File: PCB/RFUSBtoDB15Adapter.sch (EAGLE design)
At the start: 24 parts, among them IC1 S-816A40AMC-BAPT2U, J1 0, J2 AVR_SPI_PROG_3X2NS, Q2 2SA1213-Y(TE12L,F)

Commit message: PCB
PCB design updated
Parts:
- removed JP1: (no value), jumper:JP2E
- removed SJ3: (no value), jumper:SJ
- added C3, C4: 10uF, SparkFun-Capacitors:10UF-POLAR-EIA3216-16V-10%(TANT)
- R1: value 33Ω -> 80R; device eagle-ltspice:R -> SparkFun-Resistors:0.3OHM-0805-1/8W-1%
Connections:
- removed net VBUS: C1.2, C5.+, JP2.1, LED.A, R1.1
- removed net VCCIN: ARDUINO-ATMEGA328P.RAW, J1.2, J2.2, JP1.2
- new net 5VLED: LED.A, R1.1
- net 3.3V: now also ARDUINO-ATMEGA328P.VCC, C4.+; no longer JP1.3
- net 5VREG: now also C1.2, C3.+, C5.+, J1.2, J2.2, JP2.1; no longer JP1.1, SJ3.1, SJ3.2
- net GND: now also C3.-, C4.-

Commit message: PCB update
Small changes
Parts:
- renumbered ARDUINO-ATMEGA328P to ARDUINO-MINIPRO
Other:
- note removed: "IF USING A 5V ARDUINO, FEED RAW (VCCIN) PIN WITH 3.3V FROM THE REGULATOR (REG1117)."
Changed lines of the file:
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@@
 </classes>
 <parts>
-<part name="ARDUINO-ATMEGA328P" library="Arduino" deviceset="ARDUINO-PRO-MINI-*" device="" technology="5.0V"/>
+<part name="ARDUINO-MINIPRO" library="Arduino" deviceset="ARDUINO-PRO-MINI-*" device="" technology="5.0V"/>
 <part name="DB15OUT" library="dbconnector" deviceset="DB15M/90" device="" value="0"/>
 <part name="3.3V" library="burr-brown" library_urn="urn:adsk.eagle:library:111" deviceset="REG1117" device="" package3d_urn="urn:adsk.eagle:package:4940/1"/>
@@
 <sheet>
 <plain>
-<text x="45.212" y="-6.35" size="1.524" layer="113" distance="67" align="top-left">IF USING A 5V ARDUINO, FEED
-RAW (VCCIN) PIN WITH 3.3V
-FROM THE REGULATOR (REG1117).</text>
-<rectangle x1="42.418" y1="-16.002" x2="83.058" y2="-3.302" layer="203"/>
-<text x="45.72" y="-17.018" size="1.524" layer="113" distance="67" align="top-left">THE 5V REGULATOR (IC1) WILL
+<text x="-25.4" y="-17.018" size="1.524" layer="113" distance="67" align="top-left">THE 5V REGULATOR (IC1) WILL
 PROTECT THE VCC LINE FROM
 A POSSIBLE BAD PSU VOLTAGE,
 IF YOU DON'T NEED, JUST JUMPER
 SJ1.</text>
-<rectangle x1="42.418" y1="-29.21" x2="83.058" y2="-16.51" layer="203"/>
+<rectangle x1="-28.702" y1="-29.21" x2="11.938" y2="-16.51" layer="203"/>
 <text x="-46.482" y="50.546" size="1.524" layer="113" distance="67" align="top-left">FEED USB HOST SHIELD MINI VBUS WITH JP2</text>
 <rectangle x1="-49.276" y1="45.72" x2="4.064" y2="53.34" layer="203"/>
 </plain>
 <instances>
-<instance part="ARDUINO-ATMEGA328P" gate="G$1" x="-104.14" y="71.12" smashed="yes" rot="R180">
+<instance part="ARDUINO-MINIPRO" gate="G$1" x="-104.14" y="71.12" smashed="yes" rot="R180">
 <attribute name="NAME" x="-117.856" y="102.362" size="1.778" layer="95"/>
 </instance>
@@
 <instance part="C5" gate="G$1" x="9.398" y="77.47" smashed="yes" rot="R90">
 <attribute name="NAME" x="8.763" y="78.486" size="1.778" layer="95" rot="R90"/>
-<attribute name="VALUE" x="11.684" y="75.565" size="1.778" layer="96"/>
+<attribute name="VALUE" x="11.684" y="80.645" size="1.778" layer="96"/>
 </instance>
 <instance part="LOGO1" gate="G$1" x="-142.24" y="-20.32" smashed="yes"/>
@@
 </segment>
 <segment>
-<pinref part="ARDUINO-ATMEGA328P" gate="G$1" pin="D2"/>
+<pinref part="ARDUINO-MINIPRO" gate="G$1" pin="D2"/>
 <wire x1="-86.36" y1="68.58" x2="-68.58" y2="68.58" width="0.1524" layer="91"/>
 <label x="-68.58" y="68.58" size="1.778" layer="95"/>
@@
 </segment>
 <segment>
-<pinref part="ARDUINO-ATMEGA328P" gate="G$1" pin="D3"/>
+<pinref part="ARDUINO-MINIPRO" gate="G$1" pin="D3"/>
 <wire x1="-86.36" y1="71.12" x2="-68.58" y2="71.12" width="0.1524" layer="91"/>
 <label x="-68.58" y="71.12" size="1.778" layer="95"/>
@@
 </segment>
 <segment>
-<pinref part="ARDUINO-ATMEGA328P" gate="G$1" pin="D4"/>
+<pinref part="ARDUINO-MINIPRO" gate="G$1" pin="D4"/>
 <wire x1="-86.36" y1="73.66" x2="-68.58" y2="73.66" width="0.1524" layer="91"/>
 <label x="-68.58" y="73.66" size="1.778" layer="95"/>
@@
 </segment>
 <segment>
-<pinref part="ARDUINO-ATMEGA328P" gate="G$1" pin="A3"/>
+<pinref part="ARDUINO-MINIPRO" gate="G$1" pin="A3"/>
 <wire x1="-121.92" y1="68.58" x2="-139.7" y2="68.58" width="0.1524" layer="91"/>
 <label x="-142.24" y="68.58" size="1.778" layer="95"/>
@@
 <segment>
 <wire x1="-139.7" y1="71.12" x2="-121.92" y2="71.12" width="0.1524" layer="91"/>
-<pinref part="ARDUINO-ATMEGA328P" gate="G$1" pin="A2"/>
+<pinref part="ARDUINO-MINIPRO" gate="G$1" pin="A2"/>
 <label x="-144.78" y="71.12" size="1.778" layer="95"/>
 </segment>
@@
 <segment>
 <wire x1="-139.7" y1="73.66" x2="-121.92" y2="73.66" width="0.1524" layer="91"/>
-<pinref part="ARDUINO-ATMEGA328P" gate="G$1" pin="A1"/>
+<pinref part="ARDUINO-MINIPRO" gate="G$1" pin="A1"/>
 <label x="-144.78" y="73.66" size="1.778" layer="95"/>
 </segment>
@@
 <segment>
 <wire x1="-139.7" y1="76.2" x2="-121.92" y2="76.2" width="0.1524" layer="91"/>
-<pinref part="ARDUINO-ATMEGA328P" gate="G$1" pin="A0"/>
+<pinref part="ARDUINO-MINIPRO" gate="G$1" pin="A0"/>
 <label x="-144.78" y="76.2" size="1.778" layer="95"/>
 </segment>
@@
 </segment>
 <segment>
-<pinref part="ARDUINO-ATMEGA328P" gate="G$1" pin="A5"/>
+<pinref part="ARDUINO-MINIPRO" gate="G$1" pin="A5"/>
 <wire x1="-121.92" y1="50.8" x2="-142.24" y2="50.8" width="0.1524" layer="91"/>
 <label x="-149.86" y="50.8" size="1.778" layer="95"/>
 </segment>
 <segment>
-<pinref part="ARDUINO-ATMEGA328P" gate="G$1" pin="GND.3"/>
+<pinref part="ARDUINO-MINIPRO" gate="G$1" pin="GND.3"/>
 <wire x1="-121.92" y1="96.52" x2="-134.62" y2="96.52" width="0.1524" layer="91"/>
 <label x="-134.62" y="96.52" size="1.778" layer="95"/>
@@
 <net name="BUT4" class="0">
 <segment>
-<pinref part="ARDUINO-ATMEGA328P" gate="G$1" pin="D5"/>
+<pinref part="ARDUINO-MINIPRO" gate="G$1" pin="D5"/>
 <wire x1="-86.36" y1="76.2" x2="-68.58" y2="76.2" width="0.1524" layer="91"/>
 <label x="-68.58" y="76.2" size="1.778" layer="95"/>
@@
 </segment>
 <segment>
-<pinref part="ARDUINO-ATMEGA328P" gate="G$1" pin="D6"/>
+<pinref part="ARDUINO-MINIPRO" gate="G$1" pin="D6"/>
 <wire x1="-86.36" y1="78.74" x2="-68.58" y2="78.74" width="0.1524" layer="91"/>
 <label x="-68.58" y="78.74" size="1.778" layer="95"/>
@@
 <net name="BUT5" class="0">
 <segment>
-<pinref part="ARDUINO-ATMEGA328P" gate="G$1" pin="D7"/>
+<pinref part="ARDUINO-MINIPRO" gate="G$1" pin="D7"/>
 <wire x1="-86.36" y1="81.28" x2="-68.58" y2="81.28" width="0.1524" layer="91"/>
 <label x="-68.58" y="81.28" size="1.778" layer="95"/>
@@
 </segment>
 <segment>
-<pinref part="ARDUINO-ATMEGA328P" gate="G$1" pin="VCC"/>
+<pinref part="ARDUINO-MINIPRO" gate="G$1" pin="VCC"/>
 <wire x1="-121.92" y1="66.04" x2="-139.7" y2="66.04" width="0.1524" layer="91"/>
 <label x="-140.208" y="66.04" size="1.778" layer="95"/>
@@
 <net name="BUT6" class="0">
 <segment>
-<pinref part="ARDUINO-ATMEGA328P" gate="G$1" pin="A4"/>
+<pinref part="ARDUINO-MINIPRO" gate="G$1" pin="A4"/>
 <wire x1="-121.92" y1="53.34" x2="-142.24" y2="53.34" width="0.1524" layer="91"/>
 <label x="-149.86" y="53.34" size="1.778" layer="95"/>
@@
 </segment>
 <segment>
-<pinref part="ARDUINO-ATMEGA328P" gate="G$1" pin="P_GND"/>
+<pinref part="ARDUINO-MINIPRO" gate="G$1" pin="P_GND"/>
 <wire x1="-109.22" y1="35.56" x2="-109.22" y2="27.94" width="0.1524" layer="91"/>
 <label x="-109.22" y="22.86" size="1.778" layer="95" rot="R90"/>
 </segment>
 <segment>
-<pinref part="ARDUINO-ATMEGA328P" gate="G$1" pin="GND.1"/>
+<pinref part="ARDUINO-MINIPRO" gate="G$1" pin="GND.1"/>
 <wire x1="-86.36" y1="66.04" x2="-68.58" y2="66.04" width="0.1524" layer="91"/>
 <label x="-68.58" y="66.04" size="1.778" layer="95"/>
 </segment>
 <segment>
-<pinref part="ARDUINO-ATMEGA328P" gate="G$1" pin="GND.2"/>
+<pinref part="ARDUINO-MINIPRO" gate="G$1" pin="GND.2"/>
 <wire x1="-121.92" y1="60.96" x2="-142.24" y2="60.96" width="0.1524" layer="91"/>
 <label x="-147.32" y="60.96" size="1.778" layer="95"/>
@@
 <wire x1="-96.52" y1="35.56" x2="-96.52" y2="27.94" width="0.1524" layer="91"/>
 <label x="-97.028" y="27.94" size="1.778" layer="95" rot="R270"/>
-<pinref part="ARDUINO-ATMEGA328P" gate="G$1" pin="P_DTR"/>
+<pinref part="ARDUINO-MINIPRO" gate="G$1" pin="P_DTR"/>
 </segment>
 </net>
 <net name="TX" class="0">
 <segment>
-<pinref part="ARDUINO-ATMEGA328P" gate="G$1" pin="P_TXD"/>
+<pinref part="ARDUINO-MINIPRO" gate="G$1" pin="P_TXD"/>
 <wire x1="-99.06" y1="35.56" x2="-99.06" y2="27.94" width="0.1524" layer="91"/>
 <label x="-98.298" y="24.892" size="1.778" layer="95" rot="R90"/>
@@
 <net name="RX" class="0">
 <segment>
-<pinref part="ARDUINO-ATMEGA328P" gate="G$1" pin="P_RXD"/>
+<pinref part="ARDUINO-MINIPRO" gate="G$1" pin="P_RXD"/>
 <wire x1="-101.6" y1="35.56" x2="-101.6" y2="27.94" width="0.1524" layer="91"/>
 <label x="-100.584" y="24.638" size="1.778" layer="95" rot="R90"/>
@@
 <net name="RESET" class="0">
 <segment>
-<pinref part="ARDUINO-ATMEGA328P" gate="G$1" pin="RST.1"/>
+<pinref part="ARDUINO-MINIPRO" gate="G$1" pin="RST.1"/>
 <wire x1="-86.36" y1="63.5" x2="-68.58" y2="63.5" width="0.1524" layer="91"/>
 <label x="-68.58" y="63.5" size="1.778" layer="95"/>
@@
 <net name="SCK" class="0">
 <segment>
-<pinref part="ARDUINO-ATMEGA328P" gate="G$1" pin="D13"/>
+<pinref part="ARDUINO-MINIPRO" gate="G$1" pin="D13"/>
 <wire x1="-121.92" y1="78.74" x2="-127" y2="78.74" width="0.1524" layer="91"/>
 <label x="-132.08" y="78.74" size="1.778" layer="95"/>
@@
 <segment>
 <wire x1="-121.92" y1="81.28" x2="-127" y2="81.28" width="0.1524" layer="91"/>
-<pinref part="ARDUINO-ATMEGA328P" gate="G$1" pin="D12"/>
+<pinref part="ARDUINO-MINIPRO" gate="G$1" pin="D12"/>
 <label x="-132.08" y="81.28" size="1.778" layer="95"/>
 </segment>
@@
 <segment>
 <wire x1="-121.92" y1="83.82" x2="-127" y2="83.82" width="0.1524" layer="91"/>
-<pinref part="ARDUINO-ATMEGA328P" gate="G$1" pin="D11"/>
+<pinref part="ARDUINO-MINIPRO" gate="G$1" pin="D11"/>
 <label x="-132.08" y="83.82" size="1.778" layer="95"/>
 </segment>
@@
 <net name="LED" class="0">
 <segment>
-<pinref part="ARDUINO-ATMEGA328P" gate="G$1" pin="D10"/>
+<pinref part="ARDUINO-MINIPRO" gate="G$1" pin="D10"/>
 <wire x1="-121.92" y1="86.36" x2="-134.62" y2="86.36" width="0.1524" layer="91"/>
 <label x="-134.62" y="86.36" size="1.778" layer="95"/>

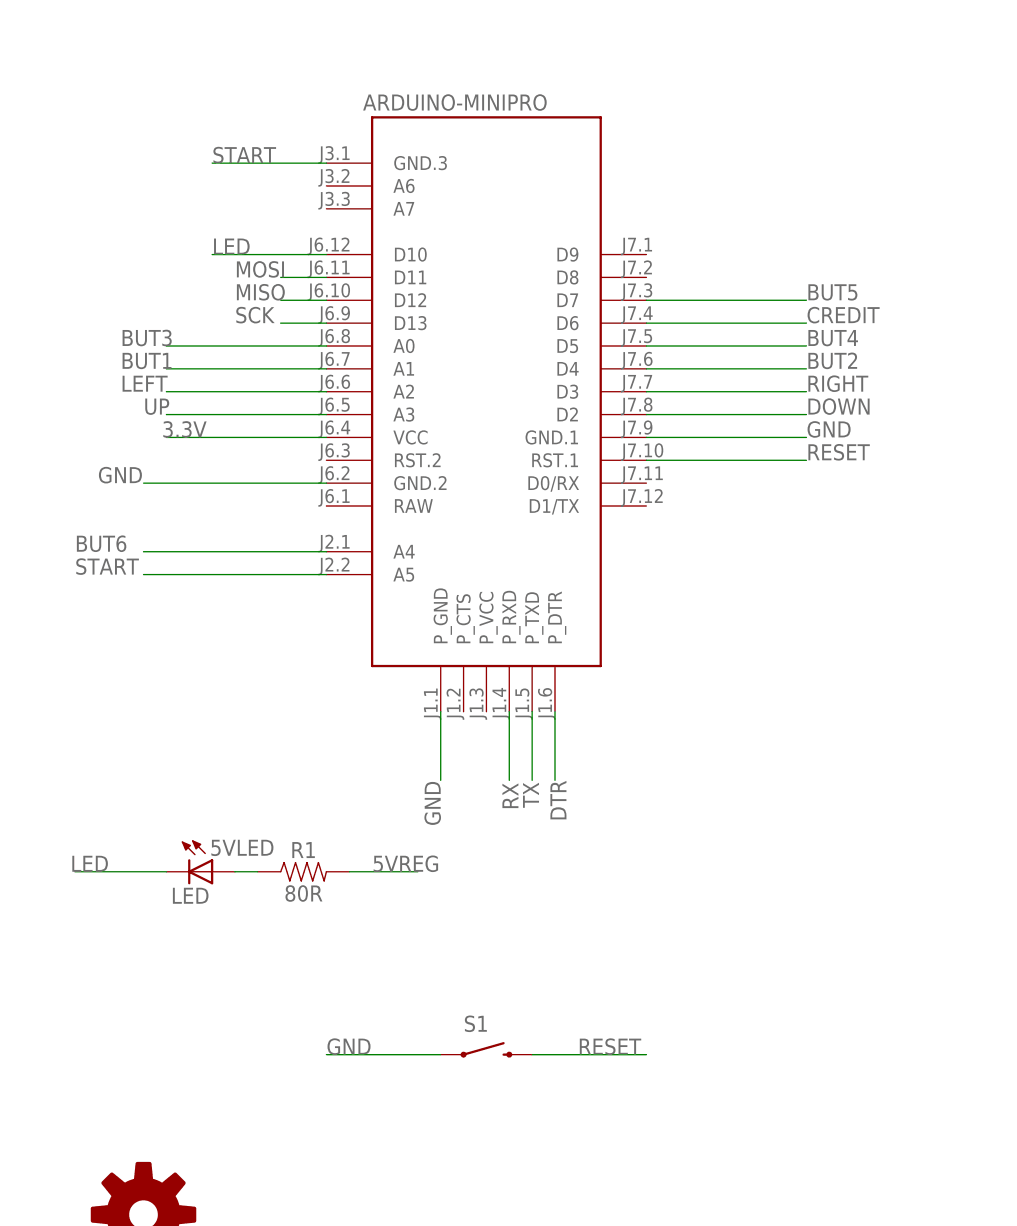
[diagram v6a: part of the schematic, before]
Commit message: PCB Update
LED status and MEMORY RESET now supported
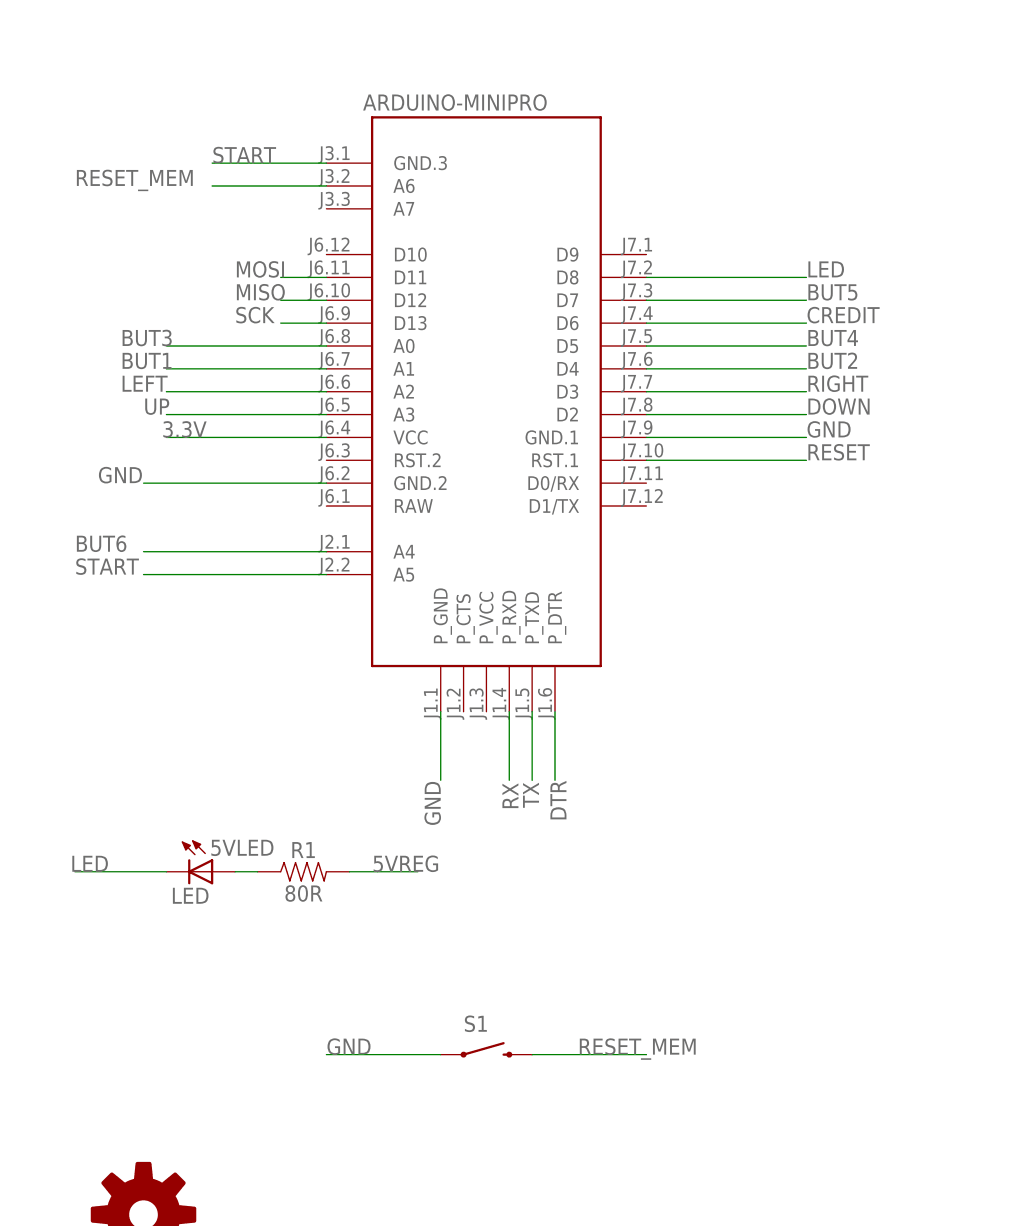
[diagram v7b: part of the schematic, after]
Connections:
- new net RESET_MEM: ARDUINO-MINIPRO.A6, S1.2
- net LED: now also ARDUINO-MINIPRO.D8; no longer ARDUINO-MINIPRO.D10
- net RESET: no longer S1.2
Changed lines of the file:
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@@
 <label x="-121.92" y="-45.72" size="1.778" layer="95"/>
-</segment>
-<segment>
-<pinref part="S1" gate="G$1" pin="2"/>
-<wire x1="-99.06" y1="-2.54" x2="-86.36" y2="-2.54" width="0.1524" layer="91"/>
-<label x="-93.98" y="-2.54" size="1.778" layer="95"/>
 </segment>
 </net>
@@
 <net name="LED" class="0">
 <segment>
-<pinref part="ARDUINO-MINIPRO" gate="G$1" pin="D10"/>
-<wire x1="-121.92" y1="86.36" x2="-134.62" y2="86.36" width="0.1524" layer="91"/>
-<label x="-134.62" y="86.36" size="1.778" layer="95"/>
-</segment>
-<segment>
 <pinref part="LED" gate="G$1" pin="C"/>
 <wire x1="-139.7" y1="17.78" x2="-149.86" y2="17.78" width="0.1524" layer="91"/>
 <label x="-150.368" y="17.78" size="1.778" layer="95"/>
+</segment>
+<segment>
+<pinref part="ARDUINO-MINIPRO" gate="G$1" pin="D8"/>
+<wire x1="-86.36" y1="83.82" x2="-68.58" y2="83.82" width="0.1524" layer="91"/>
+<label x="-68.58" y="83.82" size="1.778" layer="95"/>
 </segment>
 </net>
@@
 </segment>
 </net>
+<net name="RESET_MEM" class="0">
+<segment>
+<pinref part="ARDUINO-MINIPRO" gate="G$1" pin="A6"/>
+<wire x1="-121.92" y1="93.98" x2="-134.62" y2="93.98" width="0.1524" layer="91"/>
+<label x="-149.86" y="93.98" size="1.778" layer="95"/>
+</segment>
+<segment>
+<pinref part="S1" gate="G$1" pin="2"/>
+<wire x1="-99.06" y1="-2.54" x2="-86.36" y2="-2.54" width="0.1524" layer="91"/>
+<label x="-93.98" y="-2.54" size="1.778" layer="95"/>
+</segment>
+</net>

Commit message: PCB Update
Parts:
- removed DB15OUT: 0, dbconnector:DB15M/90
- removed PEM1, PEM2, PEM3, PEM4: KF2-M2, penn-engineering:KF2-M2
- removed R1: 80R, SparkFun-Resistors:0.3OHM-0805-1/8W-1%
- added R2: 10K, SparkFun-Resistors:0.3OHM-0805-1/8W-1%
- added R3: 500R, SparkFun-Resistors:0.3OHM-0805-1/8W-1%
- added X1: (no value), con-subd:F15HP
- C5: value 4.7UF -> 4.7uf; device resistor:CPOL-USB/3528-21W -> tantalum cap:T491A475K010AT
- LED: value (none) -> led; device adafruit:LED3MM -> led:DUOLED-RG-C
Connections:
- removed net 5VLED: LED.A, R1.1
- new net LEDREG: LED.AR, R3.2
- new net N$8: X1.9
- net 5VREG: now also C5.1, R3.1, S1.2; no longer C5.+, R1.2
- net 5VSG: now also X1.8; no longer DB15OUT.8
- net BUT1: now also X1.13; no longer DB15OUT.13
- net BUT2: now also X1.5; no longer DB15OUT.5
- net BUT3: now also X1.12; no longer DB15OUT.12
- net BUT4: now also X1.4; no longer DB15OUT.4
- net BUT5: now also X1.10; no longer DB15OUT.10
- net BUT6: now also X1.2; no longer DB15OUT.2
- net CREDIT: now also X1.3; no longer DB15OUT.3
- net DOWN: now also X1.7; no longer DB15OUT.7
- net GND: now also C5.2, R2.1, X1.1; no longer C5.-, DB15OUT.1, S1.1
- net LED: now also LED.AG; no longer LED.C
- net LEFT: now also X1.14; no longer DB15OUT.14
- net MOSI: now also LED.C
- net RESET_MEM: now also R2.2, S1.1; no longer S1.2
- net RIGHT: now also X1.6; no longer DB15OUT.6
- net START: now also X1.11; no longer DB15OUT.11
- net UP: now also X1.15; no longer DB15OUT.15
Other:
- note added: "This "START" on J3.1 PIN is just to create a new wire on the PCB design, DO NOT wire START Button on GND."
- moved on the sheet: S1
